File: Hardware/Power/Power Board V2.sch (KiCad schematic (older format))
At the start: 30 parts, among them J1 Conn_01x02, J2 Conn_01x02, J3 Conn_01x02, J4 Conn_01x02, J5 Conn_02x05_Top_Bottom

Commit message: Moved MCU Power Supply to Logic Board
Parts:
- removed C25: CP, Capacitor_THT:CP_Radial_D6.3mm_P2.50mm, symbol Device:CP
- removed R10: 8K45, Resistor_SMD:R_0603_1608Metric_Pad1.05x0.95mm_HandSolder, symbol Device:R
- removed R11: 1K15, Resistor_SMD:R_0603_1608Metric_Pad1.05x0.95mm_HandSolder, symbol Device:R
- removed R28: 25K5, Resistor_SMD:R_0603_1608Metric_Pad1.05x0.95mm_HandSolder, symbol Device:R
- J5: symbol Connector_Generic:Conn_02x05_Top_Bottom -> Connector_Generic:Conn_02x05_Odd_Even
- TP3: value +5V -> ~PWR_EN
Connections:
- net GNDPWR: now also J5.3 (Pin_3); no longer J5.4 (Pin_4)
- net VIN_FB: now also J5.1 (Pin_1); no longer J5.2 (Pin_2)
- net VOUT_FB: now also J5.2 (Pin_2); no longer J5.3 (Pin_3)
- net +5V renamed ~PWR_EN
- net ~PWR_EN: now also J5.4 (Pin_4); no longer J5.1 (Pin_1)
- net PWR_EN renamed VIN_PROTECT
- net VIN_PROTECT: now also C1.1, R22.1
- removed net VIN: C1.1, J1.2 (Pin_2), R22.1
- new net Reverse Input Protection/VIN: J1.2 (Pin_2)
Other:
- moved on the sheet: C10, H1, H2, H3, H4, J1, R22, R23, TP1

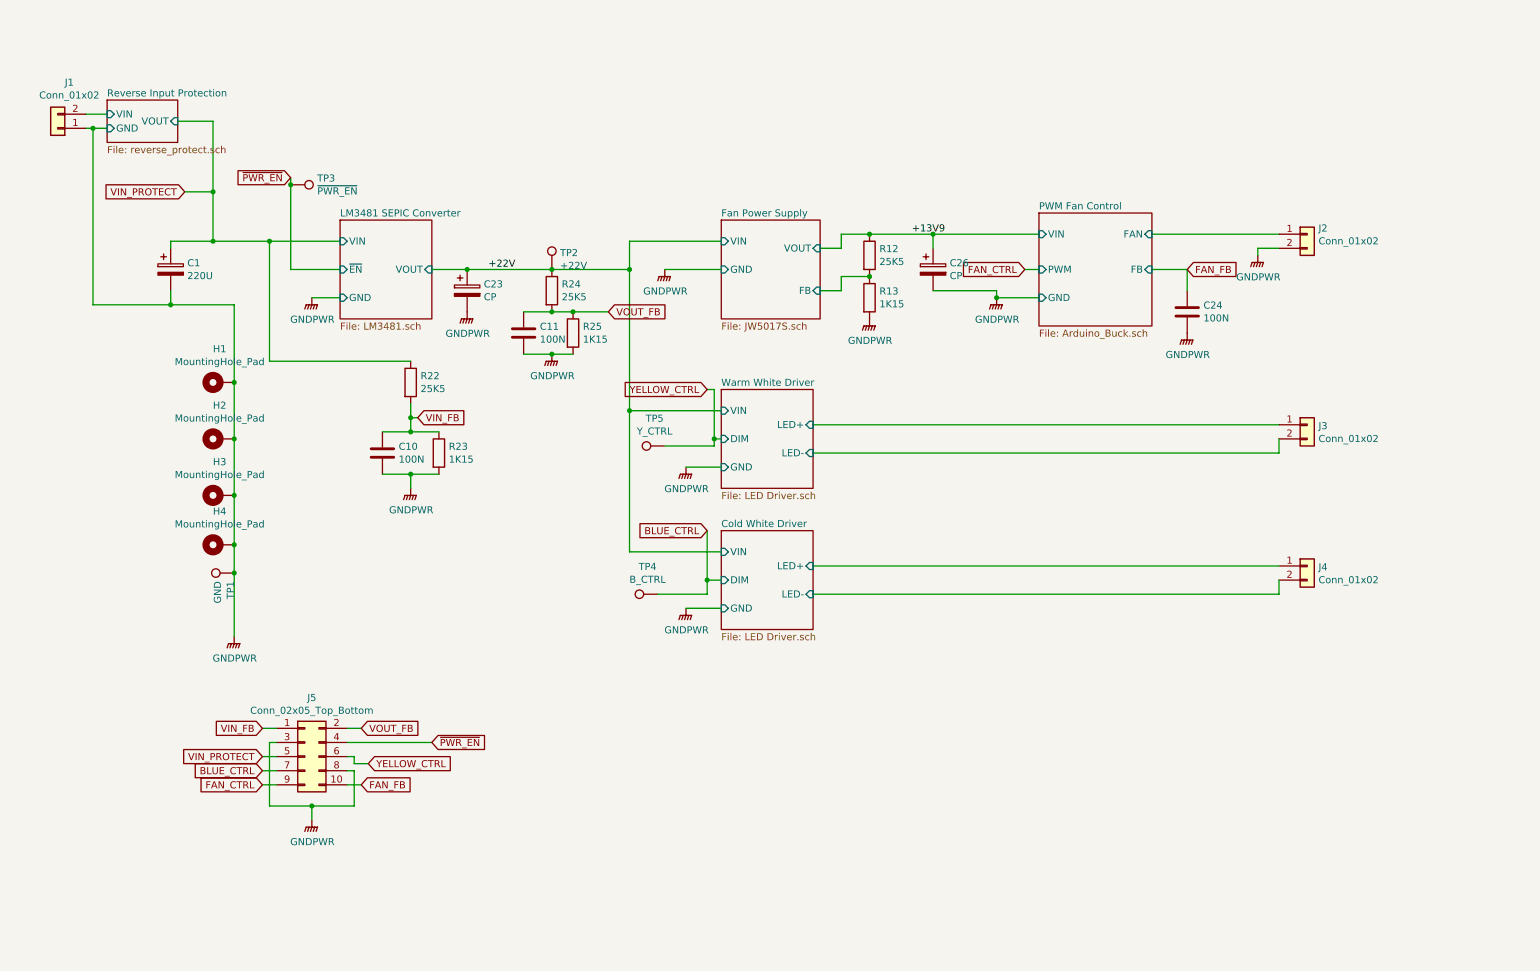
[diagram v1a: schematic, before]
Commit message: Removed Logic Board PSU from Power Board
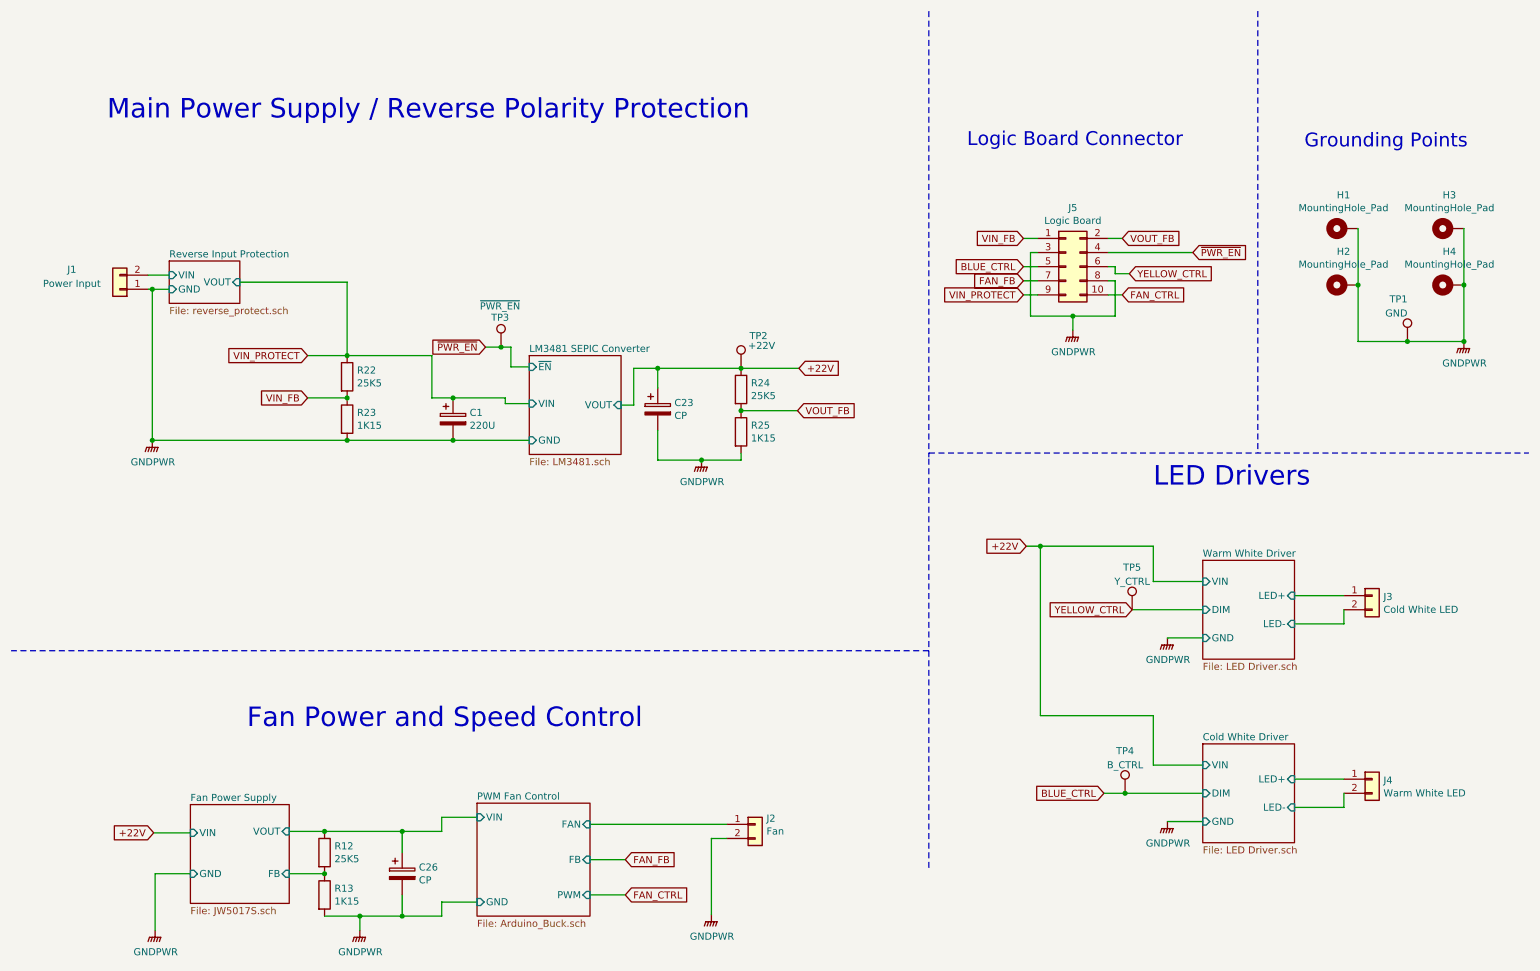
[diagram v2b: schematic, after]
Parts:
- removed C10, C11, C24: 100N, Capacitor_SMD:C_0603_1608Metric_Pad1.05x0.95mm_HandSolder, symbol Device:C
- J1: value Conn_01x02 -> Power Input
- J2: value Conn_01x02 -> Fan
- J3: value Conn_01x02 -> Cold White LED
- J4: value Conn_01x02 -> Warm White LED
- J5: value Conn_02x05_Top_Bottom -> Logic Board
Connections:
- net BLUE_CTRL: now also J5.5 (Pin_5); no longer J5.7 (Pin_7)
- net FAN_CTRL: now also J5.10 (Pin_10); no longer J5.9 (Pin_9)
- net FAN_FB: now also J5.7 (Pin_7); no longer J5.10 (Pin_10)
- net VIN_PROTECT: now also J5.9 (Pin_9); no longer J5.5 (Pin_5)
- net +13V9 renamed Fan Power Supply/VOUT
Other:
- note added: "Fan Power and Speed Control"
- note added: "Grounding Points"
- note added: "LED Drivers"
- note added: "Logic Board Connector"
- note added: "Main Power Supply / Reverse Polarity Protection"
- moved on the sheet: C1, C23, C26, H1, H2, H3, H4, J1, J2, J3, J4, J5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
